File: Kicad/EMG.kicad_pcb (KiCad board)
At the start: 0 parts

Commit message: Se inició con el Pcb. Se eliminó el capacitor del socket del nrf. Se cambió el conector de la bat.
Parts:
- added C1: 10nF, EMG:C_0805, B.Cu at (186.3, 77.7)
- added C10: C, EMG:C_0805, B.Cu at (226.6, 84.4)
- added C11: C, EMG:C_0805, F.Cu at (230.4, 55.7)
- added C2: 0.33uF, EMG:C_0805, B.Cu at (199.0, 84.0)
- added C3: 0.33uF, EMG:C_0805, B.Cu at (177.0, 74.8)
- added C4: 1uF, EMG:C_0805, B.Cu at (182.2, 81.1)
- added C5: 0.68uF, EMG:C_0805, B.Cu at (190.7, 90.2)
- added C6: 1uF, EMG:C_0805, B.Cu at (186.3, 84.0)
- added C7: CP, EMG:C_0805, F.Cu at (230.5, 47.9)
- added C8: CP, EMG:C_0805, F.Cu at (230.4, 51.8)
- added C9: C, EMG:C_0805, B.Cu at (178.0, 53.0)
- added D1: LED, EMG:Pin_Header_Straight_1x02_Pitch2.54mm, F.Cu at (203.2, 57.2)
- added IC1: MAX8881EUT33-T, EMG:sot23-6, F.Cu at (219.2, 48.3)
- added P1: nRF24l01, EMG:Pin_Header_Straight_1x08_Pitch1.27mm, F.Cu at (224.2, 42.7)
- added P2: CONN_01X02, EMG:Pin_Header_Straight_1x02_Pitch2.54mm, B.Cu at (232.0, 71.5)
- added P3: USB_A, EMG:usb_vert, F.Cu at (211.4, 50.8)
- added P4: CONN_01X05, EMG:Pin_Header_Straight_1x05_Pitch2.54mm, B.Cu at (170.9, 61.8)
- added P5: CONN_01X03, EMG:Pin_Header_Straight_1x03_Pitch2.54mm, F.Cu at (202.7, 42.7)
- added R1: 10K, EMG:R_0805, B.Cu at (181.6, 74.8)
- added R10: 1M, EMG:R_0805, B.Cu at (194.4, 77.7)
- added R11: 1M, EMG:R_0805, B.Cu at (208.4, 90.2)
- added R12: 43K, EMG:R_0805, B.Cu at (203.6, 84.0)
- added R13: 430K, EMG:R_0805, B.Cu at (190.4, 77.7)
- added R14: 430K, EMG:R_0805, B.Cu at (204.4, 90.2)
- added R15: 43K, EMG:R_0805, B.Cu at (200.5, 90.2)
- added R16: 43K, EMG:R_0805, B.Cu at (186.1, 90.2)
- added R17: 215K, EMG:R_0805, B.Cu at (194.1, 84.0)
- added R18: 215K, EMG:R_0805, B.Cu at (185.5, 71.5)
- added R19: 10M, EMG:R_0805, B.Cu at (190.2, 84.0)
- added R2: 510K, EMG:R_0805, B.Cu at (178.1, 81.1)
- added R20: 1600K, EMG:R_0805, B.Cu at (196.0, 90.2)
- added R21: R, EMG:R_0805, F.Cu at (225.5, 51.8)
- added R22: R, EMG:R_0805, F.Cu at (225.5, 47.9)
- added R3: 43K, EMG:R_0805, B.Cu at (200.4, 71.5)
- added R4: 43K, EMG:R_0805, B.Cu at (196.8, 71.5)
- added R5: 22K, EMG:R_0805, B.Cu at (207.2, 84.0)
- added R6: 22K, EMG:R_0805, B.Cu at (193.1, 71.5)
- added R7: 10M, EMG:R_0805, B.Cu at (201.7, 77.7)
- added R8: 10M, EMG:R_0805, B.Cu at (198.0, 77.7)
- added R9: 10M, EMG:R_0805, B.Cu at (189.5, 71.5)
- added SW1: SW_PUSH, EMG:Pin_Header_Straight_1x02_Pitch2.54mm, B.Cu at (240.7, 71.5)
- added U1: MSP430G2231IPW14, EMG:TSSOP-14_4.4x5mm_Pitch0.65mm, B.Cu at (183.8, 60.7)
- added U2: TLC2274, EMG:TSSOP-14_4.4x5mm_Pitch0.65mm, B.Cu at (180.1, 88.8)
- added U3: TLC2274, EMG:TSSOP-14_4.4x5mm_Pitch0.65mm, B.Cu at (170.1, 76.9)
- added U4: MCP73831, EMG:sot23-5, F.Cu at (219.2, 54.6)
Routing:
- net (no net): track 0.00 -> 5.54 mm
- net Net-(C7-Pad1): track 0.00 -> 1.00 mm
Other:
- board outline added: 35 x 23 mm
- copper layers 0 -> 2
- net class Default added: clearance 0.2, trace_width 0.25, via_dia 0.6, via_drill 0.4

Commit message: Se continua el pcb
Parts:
- added C12: C, EMG:C_0805, F.Cu at (125.3, 110.1)
- C1, C10, C2, C3, C4, C5, C6, C9, P2, P4, R1, R10, R11, R12, R13, R14, R15, R16, R17, R18, R19, R2, R20, R3, R4, R5, R6, R7, R8, R9, SW1, U1, U2, U3: moved to F.Cu
- moved C7 143.3 mm to (102.7, 112.7)
- moved C8 138.1 mm to (106.5, 112.7), turned to 180 degrees
- moved C11 137.2 mm to (106.5, 114.7), turned to 180 degrees
- moved R22 135.4 mm to (109.6, 117.9), turned to 90 degrees
- moved SW1 133.4 mm to (110.1, 98.5), turned to 270 degrees
- moved U4 132.8 mm to (102.4, 117.7)
- moved IC1 132.7 mm to (106.1, 117.7), turned to 180 degrees
- moved R21 131.2 mm to (112.2, 117.9), turned to 270 degrees
- moved C10 127.6 mm to (102.7, 114.7)
- moved P3 122.8 mm to (101.6, 105.7)
- moved P2 118.9 mm to (116.2, 98.5), turned to 270 degrees
- moved P1 110.3 mm to (129.0, 98.5)
- moved D1 90.7 mm to (122.5, 98.5), turned to 270 degrees
- moved P4 67.2 mm to (134.0, 117.9), turned to 270 degrees
- moved U1 66.3 mm to (134.2, 104.6), turned to 270 degrees
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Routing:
- net (no net): track 5.54 -> 0.00 mm
- net Net-(C7-Pad1): track 1.00 -> 0.00 mm
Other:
- board outline removed

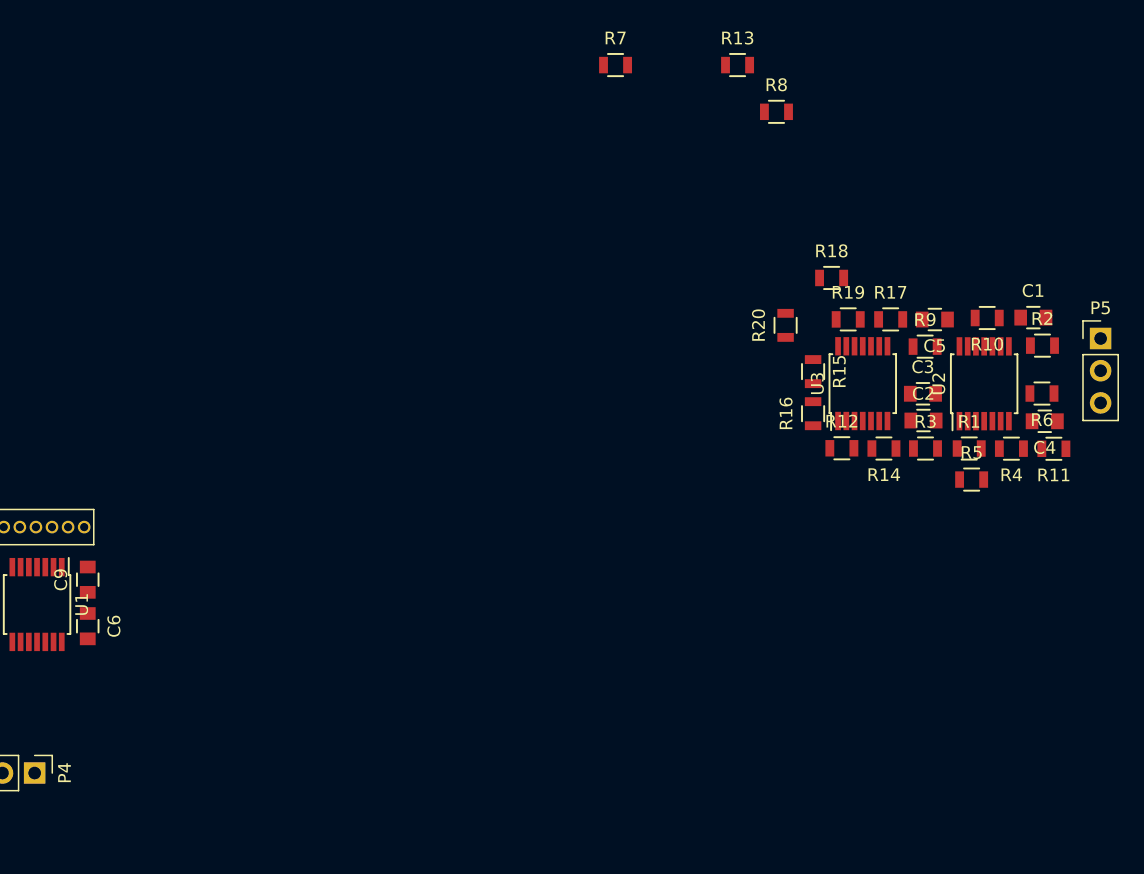
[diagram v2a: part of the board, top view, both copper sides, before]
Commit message: Ruteo de etapa de adquisición
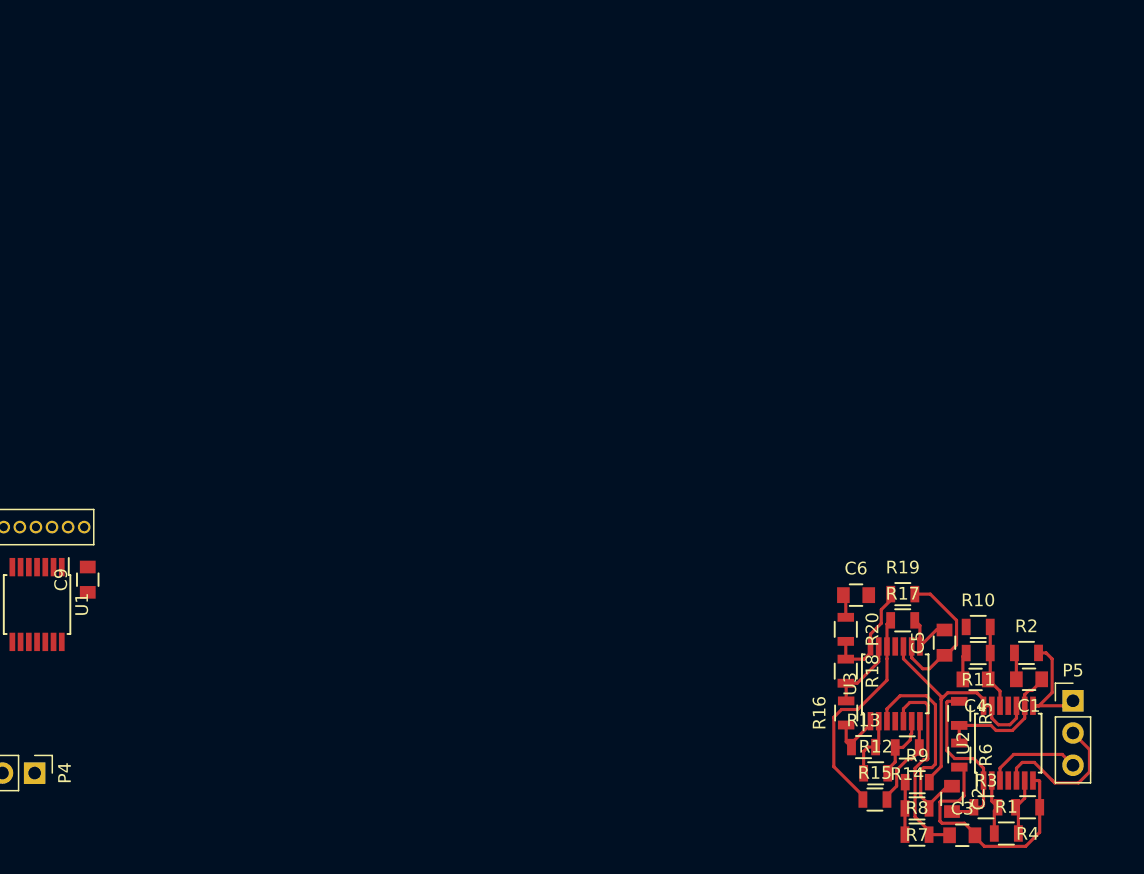
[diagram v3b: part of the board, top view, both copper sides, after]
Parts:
- moved R7 63.3 mm to (203.6, 120.7), turned to 180 degrees
- moved C6 60.7 mm to (198.8, 103.9), turned to 0 degrees
- moved R8 58.1 mm to (203.6, 122.8)
- moved R13 54.7 mm to (199.4, 115.9)
- moved C3 35.0 mm to (207.2, 122.8)
- moved R9 34.4 mm to (203.6, 118.7)
- moved R15 34.1 mm to (200.3, 120.0), turned to 0 degrees
- moved R18 31.1 mm to (198.0, 109.9), turned to 270 degrees
- moved R1 30.5 mm to (210.7, 122.7)
- moved C2 29.9 mm to (206.4, 120.0), turned to 270 degrees
- moved R6 29.3 mm to (207.0, 116.5), turned to 270 degrees
- moved R3 28.7 mm to (209.1, 120.6)
- moved P5 28.7 mm to (215.9, 112.2)
- moved C1 28.5 mm to (212.5, 110.5), turned to 180 degrees
- moved U2 28.4 mm to (210.8, 115.6)
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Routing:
- net Net-(R9-Pad2): track 0.00 -> 21.6 mm
- net Net-(C3-Pad2): track 0.00 -> 20.1 mm
- net Net-(R15-Pad1): track 0.00 -> 17.7 mm
- net Net-(C2-Pad1): track 0.00 -> 17.2 mm
- net Net-(C3-Pad1): track 0.00 -> 16.1 mm
- net Net-(C2-Pad2): track 0.00 -> 13.9 mm
- net Net-(C5-Pad1): track 0.00 -> 11.7 mm
- net Net-(P5-Pad2): track 0.00 -> 11.6 mm
- net Net-(C1-Pad1): track 0.00 -> 10.9 mm
- net Net-(P5-Pad1): track 0.00 -> 9.19 mm
- net Net-(R18-Pad1): track 0.00 -> 8.85 mm
- net Net-(P5-Pad3): track 0.00 -> 7.54 mm
- net Net-(R14-Pad1): track 0.00 -> 7.43 mm
- net Net-(C4-Pad1): track 0.00 -> 6.67 mm
- net Net-(R16-Pad2): track 0.00 -> 5.92 mm
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
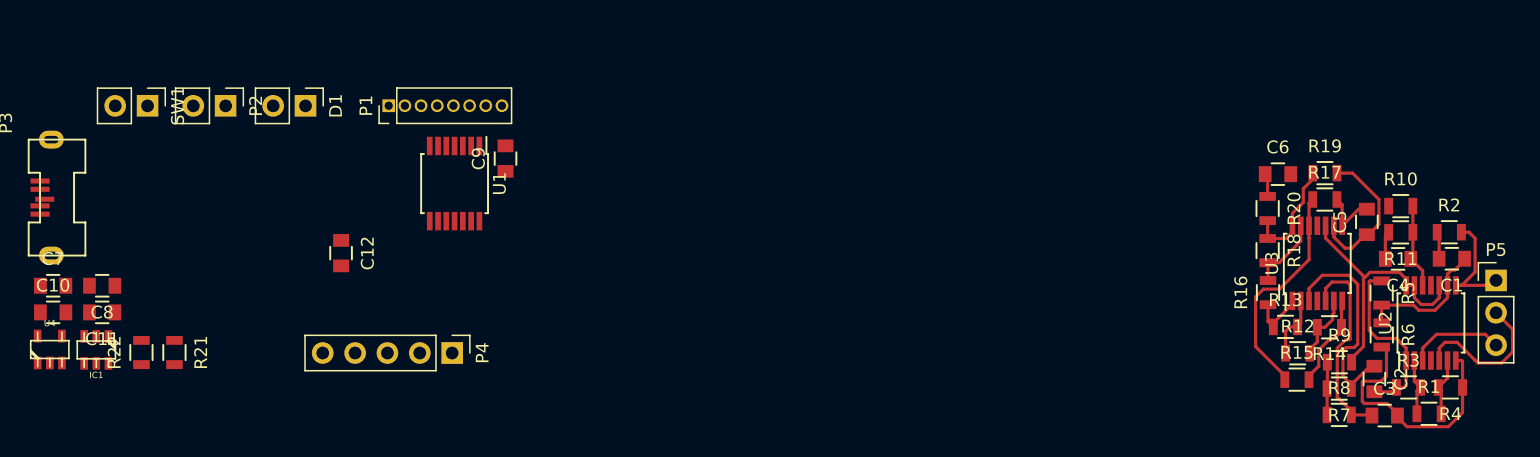
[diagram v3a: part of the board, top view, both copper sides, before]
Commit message: Reglas de diseño Mayer10mils
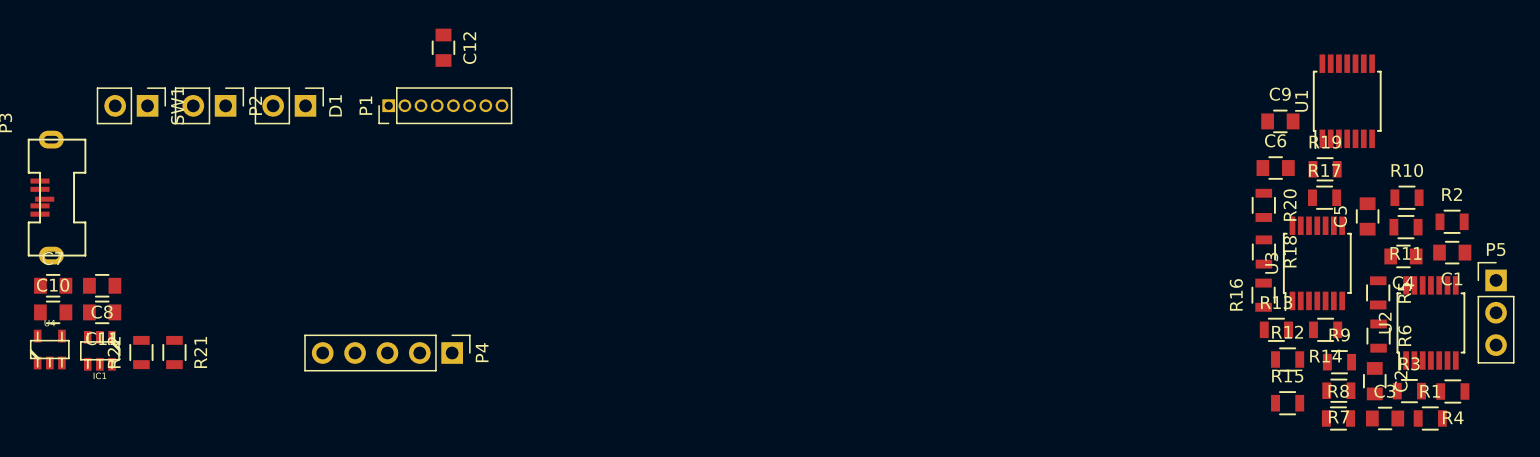
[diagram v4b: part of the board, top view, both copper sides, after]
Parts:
- moved U1 70.4 mm to (204.2, 98.2), turned to 90 degrees
- moved C9 60.9 mm to (199.0, 99.8), turned to 0 degrees
- moved C12 18.0 mm to (133.3, 94.0)
- moved R15 1.99 mm to (199.6, 121.9)
- moved R12 0.93 mm to (199.6, 118.4)
- moved R2 0.85 mm to (212.5, 107.6)
- moved R10 0.82 mm to (208.9, 105.7)
- moved R13 0.75 mm to (198.7, 116.1)
- moved R11 0.58 mm to (208.9, 108.0)
- moved C6 0.51 mm to (198.6, 103.4)
- moved C1 0.48 mm to (212.5, 110.0)
- moved C4 0.46 mm to (208.7, 110.3)
- moved C5 0.43 mm to (205.8, 107.2)
- moved R16 0.40 mm to (197.7, 113.4)
- moved R20 0.39 mm to (197.7, 106.3)
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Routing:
- net Net-(R9-Pad2): track 21.6 -> 0.00 mm
- net Net-(C3-Pad2): track 20.1 -> 0.00 mm
- net Net-(R15-Pad1): track 17.7 -> 0.00 mm
- net Net-(C2-Pad1): track 17.2 -> 0.00 mm
- net Net-(C3-Pad1): track 16.1 -> 0.00 mm
- net Net-(C2-Pad2): track 13.9 -> 0.00 mm
- net Net-(C5-Pad1): track 11.7 -> 0.00 mm
- net Net-(P5-Pad2): track 11.6 -> 0.00 mm
- net Net-(C1-Pad1): track 10.9 -> 0.01 mm
- net Net-(R18-Pad1): track 8.85 -> 0.00 mm
- net Net-(P5-Pad1): track 9.19 -> 0.55 mm
- net Net-(P5-Pad3): track 7.54 -> 0.00 mm
- net Net-(R14-Pad1): track 7.43 -> 0.00 mm
- net Net-(C4-Pad1): track 6.67 -> 0.00 mm
- net Net-(R16-Pad2): track 5.92 -> 0.00 mm
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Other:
- net class Mayer10mils added: clearance 0.25, trace_width 0.25, via_dia 1, via_drill 0.5

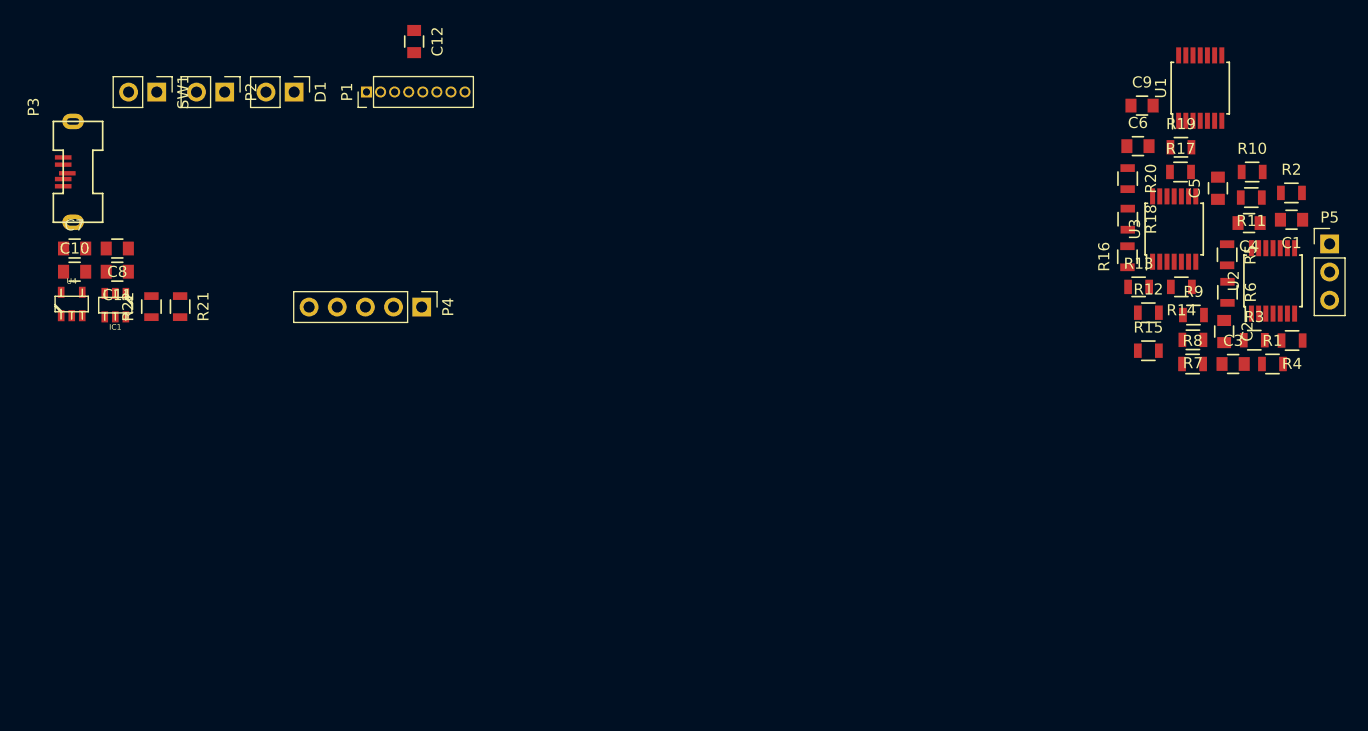
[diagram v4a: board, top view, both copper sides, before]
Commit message: Cambios en tamaño de pinheaders
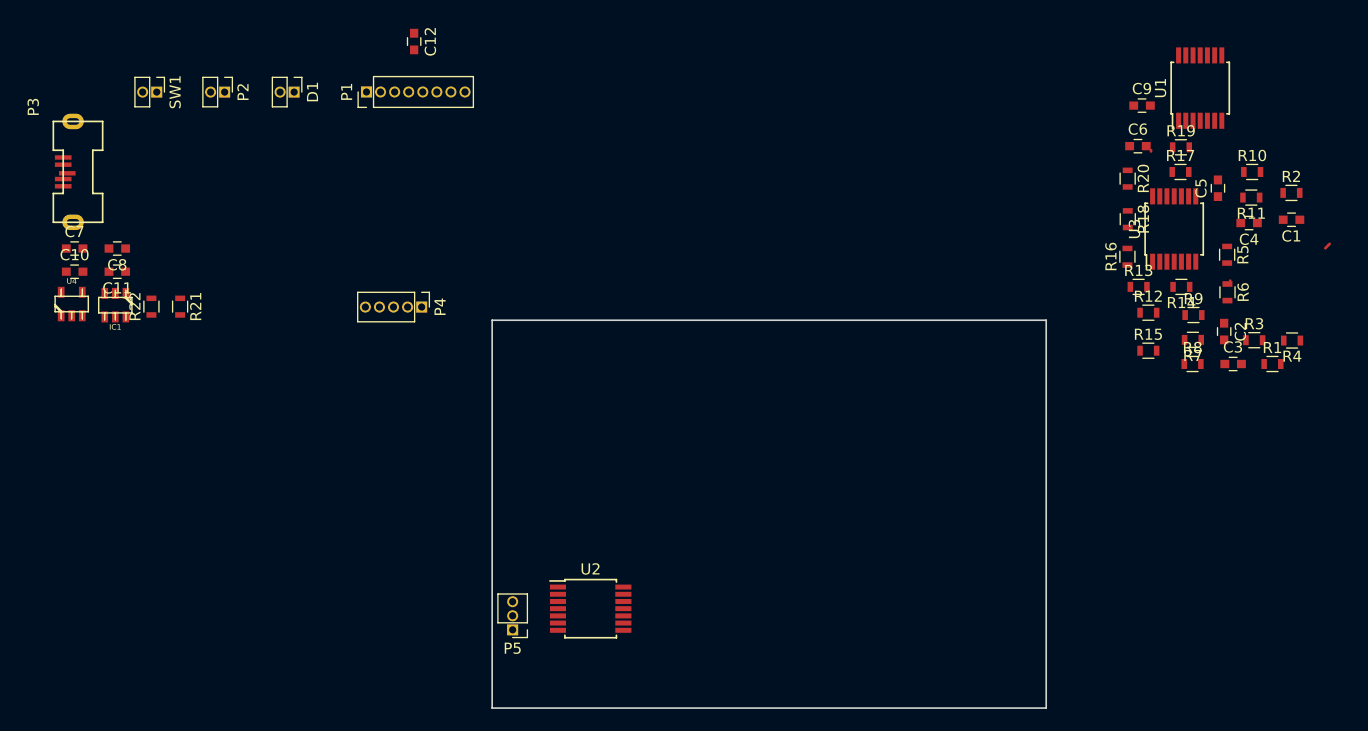
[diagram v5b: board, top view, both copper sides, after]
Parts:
- C1, C10, C11, C12, C2, C3, C4, C5, C6, C7, C8, C9: footprint EMG:C_0805 -> EMG:C_0603
- D1, P2, SW1: footprint EMG:Pin_Header_Straight_1x02_Pitch2.54mm -> EMG:Pin_Header_Straight_1x02_Pitch1.27mm
- P4: footprint EMG:Pin_Header_Straight_1x05_Pitch2.54mm -> EMG:Pin_Header_Straight_1x05_Pitch1.27mm
- P5: footprint EMG:Pin_Header_Straight_1x03_Pitch2.54mm -> EMG:Pin_Header_Straight_1x03_Pitch1.27mm
- R1, R10, R11, R12, R13, R14, R15, R16, R17, R18, R19, R2, R20, R21, R22, R3, R4, R5, R6, R7, R8, R9: footprint EMG:R_0805 -> EMG:R_0603
- moved P5 81.5 mm to (142.2, 147.1), turned to 180 degrees
- moved U2 68.3 mm to (149.2, 145.2), turned to 0 degrees
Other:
- board outline added: 50 x 35 mm

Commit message: Ruteo pcb
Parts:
- P1: footprint EMG:Pin_Header_Straight_1x08_Pitch1.27mm -> EMG:nRF
- moved C1 72.6 mm to (143.2, 131.5)
- moved R2 71.5 mm to (143.2, 125.4)
- moved R10 69.4 mm to (146.3, 135.7), turned to 90 degrees
- moved U1 68.3 mm to (158.9, 149.2), turned to 270 degrees
- moved R11 66.2 mm to (148.7, 135.7), turned to 270 degrees
- moved R5 66.2 mm to (143.9, 134.4), turned to 90 degrees
- moved P3 65.2 mm to (155.6, 142.3), turned to 180 degrees
- moved R6 63.9 mm to (143.9, 128.5), turned to 90 degrees
- moved C4 62.8 mm to (151.2, 135.7), turned to 270 degrees
- moved R4 59.5 mm to (153.4, 127.4), turned to 90 degrees
- moved C9 59.0 mm to (166.4, 148.9), turned to 90 degrees
- moved R3 57.3 mm to (151.8, 122.4), turned to 270 degrees
- moved R1 56.6 mm to (154.2, 124.0), turned to 270 degrees
- moved C5 55.6 mm to (159.0, 137.1), turned to 180 degrees
- moved R17 53.4 mm to (157.5, 134.5), turned to 270 degrees
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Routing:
- net Net-(C2-Pad2): track 0.00 -> 33.2 mm
- net GND: track 0.00 -> 23.5 mm, vias 0 -> 2
- net Net-(R9-Pad2): track 0.00 -> 22.4 mm
- net Net-(C2-Pad1): track 0.00 -> 20.9 mm
- net Net-(R15-Pad1): track 0.00 -> 18.9 mm
- net Net-(C3-Pad2): track 0.00 -> 15.5 mm
- net Net-(R18-Pad1): track 0.00 -> 14.8 mm
- net Net-(P5-Pad1): track 0.55 -> 13.9 mm
- net Net-(R16-Pad2): track 0.00 -> 11.3 mm
- net Net-(R1-Pad2): track 0.00 -> 10.8 mm
- net Net-(C3-Pad1): track 0.00 -> 10.4 mm
- net Net-(C1-Pad1): track 0.00 -> 9.00 mm
- net Net-(R1-Pad1): track 0.00 -> 8.63 mm
- net Net-(C4-Pad1): track 0.00 -> 8.40 mm
- net Net-(C5-Pad2): track 0.00 -> 7.08 mm
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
